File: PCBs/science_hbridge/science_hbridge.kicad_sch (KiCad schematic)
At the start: 32 parts, among them J1 Conn_02x07_Odd_Even, J2 Conn_02x08_Odd_Even, J3 Conn_02x08_Odd_Even, J4 Conn_01x02_Pin, J5 Conn_01x02_Pin, J6 Conn_01x02_Pin, J7 Conn_01x04_Pin, U1 L298N, U2 MAX485E, U3 NCP718xSN500

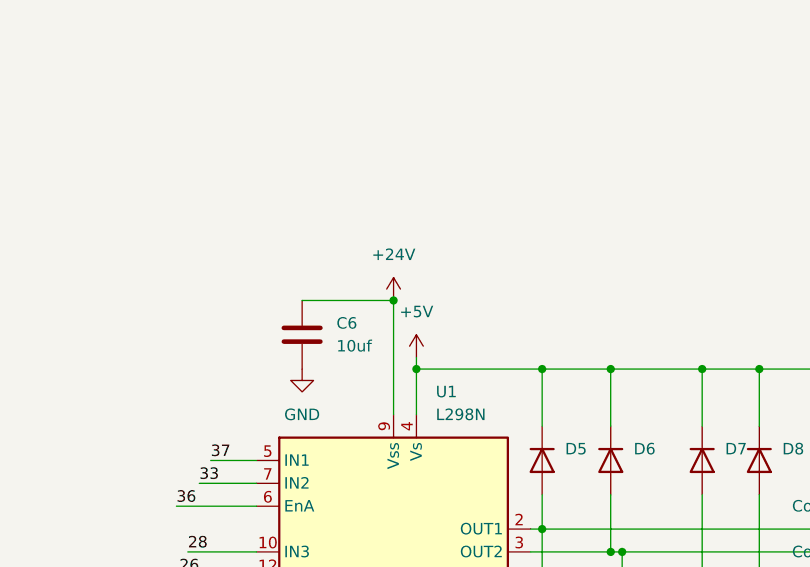
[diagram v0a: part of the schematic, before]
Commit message: fixed errors, need to add quadrature
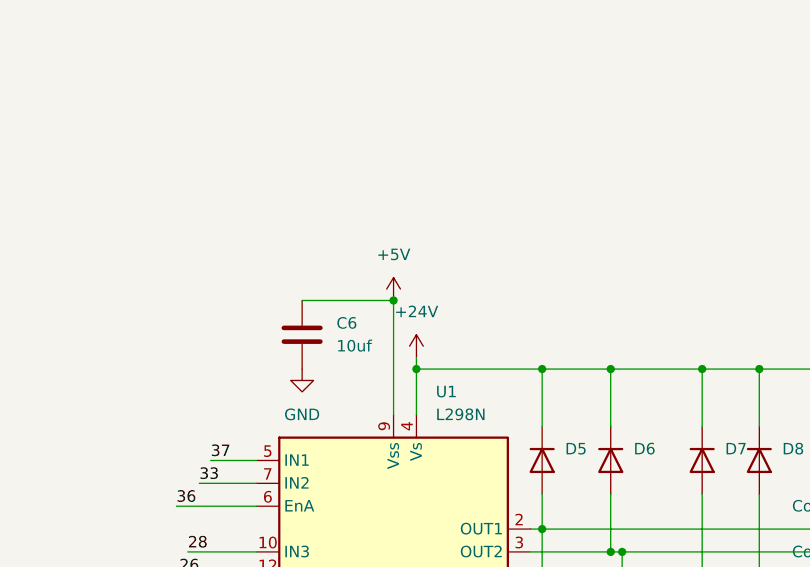
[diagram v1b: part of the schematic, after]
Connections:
- net +24V: now also C1.1, C2.1, D5.1 (K), D6.1 (K), D7.1 (K), D8.1 (K), U1.4 (Vs); no longer C6.1, U1.9 (Vss)
- net +5V: now also C6.1, U1.9 (Vss); no longer C1.1, C2.1, D5.1 (K), D6.1 (K), D7.1 (K), D8.1 (K), U1.4 (Vs)
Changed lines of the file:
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@@
 	)
 	(junction
+		(at 295.91 157.48)
+		(diameter 0)
+		(color 0 0 0 0)
+	)
+	(junction
 		(at 312.42 165.1)
 		(diameter 0)
@@
 	)
 	(junction
-		(at 295.91 157.48)
-		(diameter 0)
-		(color 0 0 0 0)
-	)
-	(junction
 		(at 364.49 172.72)
 		(diameter 0)
@@
 	(symbol
 		(lib_id "power:+3.3V")
-		(at 298.45 163.83 0)
+		(at 295.91 157.48 0)
 		(unit 1)
 		(exclude_from_sim no)
@@
 		(fields_autoplaced yes)
 		(property "Reference" "#PWR01"
-			(at 298.45 167.64 0)
+			(at 295.91 161.29 0)
 			(effects
 				(font
@@
 		)
 		(property "Value" "+5V"
-			(at 298.45 158.75 0)
+			(at 295.91 152.4 0)
 			(effects
 				(font
@@
 		)
 		(property "Footprint" ""
-			(at 298.45 163.83 0)
+			(at 295.91 157.48 0)
 			(effects
 				(font
@@
 		)
 		(property "Datasheet" ""
-			(at 298.45 163.83 0)
+			(at 295.91 157.48 0)
 			(effects
 				(font
@@
 		)
 		(property "Description" "Power symbol creates a global label with name \"+3.3V\""
-			(at 298.45 163.83 0)
+			(at 295.91 157.48 0)
 			(effects
 				(font
@@
 	(symbol
 		(lib_id "power:+3.3V")
-		(at 295.91 157.48 0)
+		(at 298.45 163.83 0)
 		(unit 1)
 		(exclude_from_sim no)
@@
 		(fields_autoplaced yes)
 		(property "Reference" "#PWR016"
-			(at 295.91 161.29 0)
+			(at 298.45 167.64 0)
 			(effects
 				(font
@@
 		)
 		(property "Value" "+24V"
-			(at 295.91 152.4 0)
+			(at 298.45 158.75 0)
 			(effects
 				(font
@@
 		)
 		(property "Footprint" ""
-			(at 295.91 157.48 0)
+			(at 298.45 163.83 0)
 			(effects
 				(font
@@
 		)
 		(property "Datasheet" ""
-			(at 295.91 157.48 0)
+			(at 298.45 163.83 0)
 			(effects
 				(font
@@
 		)
 		(property "Description" "Power symbol creates a global label with name \"+3.3V\""
-			(at 295.91 157.48 0)
+			(at 298.45 163.83 0)
 			(effects
 				(font

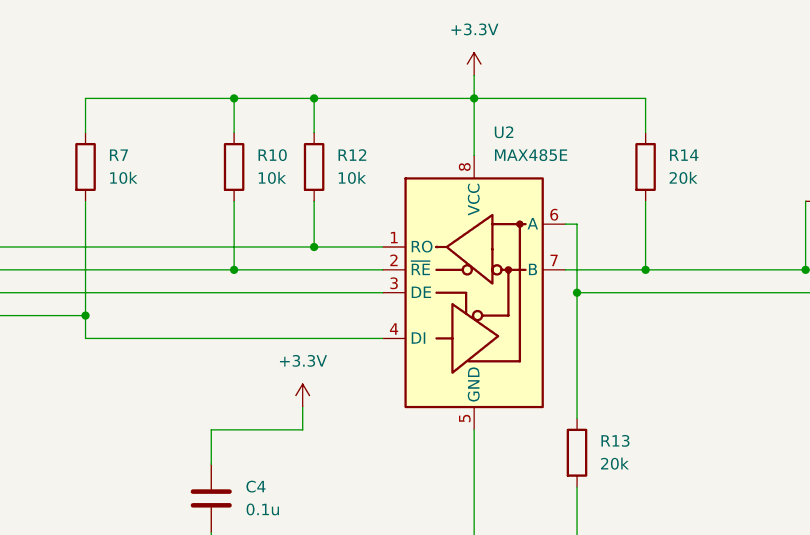
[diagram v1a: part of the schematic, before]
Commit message: fixed both boards, just needs mounting + silkscreen, ready to review
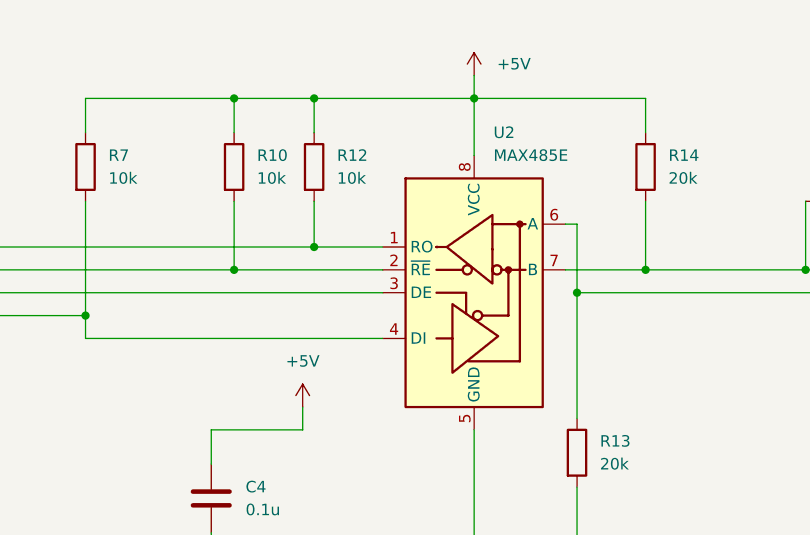
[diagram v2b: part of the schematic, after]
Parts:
- J4, J5: footprint Connector_JST:JST_XH_S2B-XH-A_1x02_P2.50mm_Horizontal -> Connector_JST:JST_GH_SM02B-GHS-TB_1x02-1MP_P1.25mm_Horizontal
- J6: footprint Connector_JST:JST_XH_S2B-XH-A_1x02_P2.50mm_Horizontal -> Connector_Molex:Molex_Micro-Fit_3.0_43045-0212_2x01_P3.00mm_Vertical
- J7: footprint Connector_JST:JST_XH_S4B-XH-A_1x04_P2.50mm_Horizontal -> Connector_JST:JST_GH_SM04B-GHS-TB_1x04-1MP_P1.25mm_Horizontal
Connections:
- net +3.3V: no longer C4.1, R10.1, R12.1, R14.1, R7.1, U2.8 (VCC)
- net +5V: now also C4.1, R10.1, R12.1, R14.1, R7.1, U2.8 (VCC)
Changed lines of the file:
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@@
 			)
 		)
-		(property "Value" "+3.3V"
+		(property "Value" "+5V"
 			(at 292.1 82.55 0)
 			(effects
@@
 			)
 		)
-		(property "Footprint" "Connector_JST:JST_XH_S2B-XH-A_1x02_P2.50mm_Horizontal"
+		(property "Footprint" "Connector_JST:JST_GH_SM02B-GHS-TB_1x02-1MP_P1.25mm_Horizontal"
 			(at 347.98 187.96 0)
 			(effects
@@
 			)
 		)
-		(property "Footprint" "Connector_JST:JST_XH_S4B-XH-A_1x04_P2.50mm_Horizontal"
+		(property "Footprint" "Connector_JST:JST_GH_SM04B-GHS-TB_1x04-1MP_P1.25mm_Horizontal"
 			(at 369.57 74.93 0)
 			(effects
@@
 			)
 		)
-		(property "Footprint" "Connector_JST:JST_XH_S2B-XH-A_1x02_P2.50mm_Horizontal"
+		(property "Footprint" "Connector_JST:JST_GH_SM02B-GHS-TB_1x02-1MP_P1.25mm_Horizontal"
 			(at 347.98 182.88 0)
 			(effects
@@
 			)
 		)
-		(property "Value" "+3.3V"
-			(at 311.15 45.72 0)
-			(effects
-				(font
-					(size 1.27 1.27)
-				)
+		(property "Value" "+5V"
+			(at 313.69 49.5299 0)
+			(effects
+				(font
+					(size 1.27 1.27)
+				)
+				(justify left)
 			)
 		)
@@
 			)
 		)
-		(property "Footprint" "Connector_JST:JST_XH_S2B-XH-A_1x02_P2.50mm_Horizontal"
+		(property "Footprint" "Connector_Molex:Molex_Micro-Fit_3.0_43045-0212_2x01_P3.00mm_Vertical"
 			(at 458.47 81.28 0)
 			(effects
